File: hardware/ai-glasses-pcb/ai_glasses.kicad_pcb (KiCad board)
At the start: 4 copper layers, 116 x 22 mm, 55 parts, among them J1 USB-C, J2 CAMERA DVP, J3 LiPo 1S, Q1 DMG3415U, SW1 BOOT, SW2 RESET, U1 ESP32-S3-WROOM-1-N16R8, U2 MCP73831-2-OT, U3 AP2112K-3.3, U4 TLV70028DDCR, U5 TLV70012DDCR, U6 ICS-43434, U7 MAX98357A, U8 USBLC6-2SC6

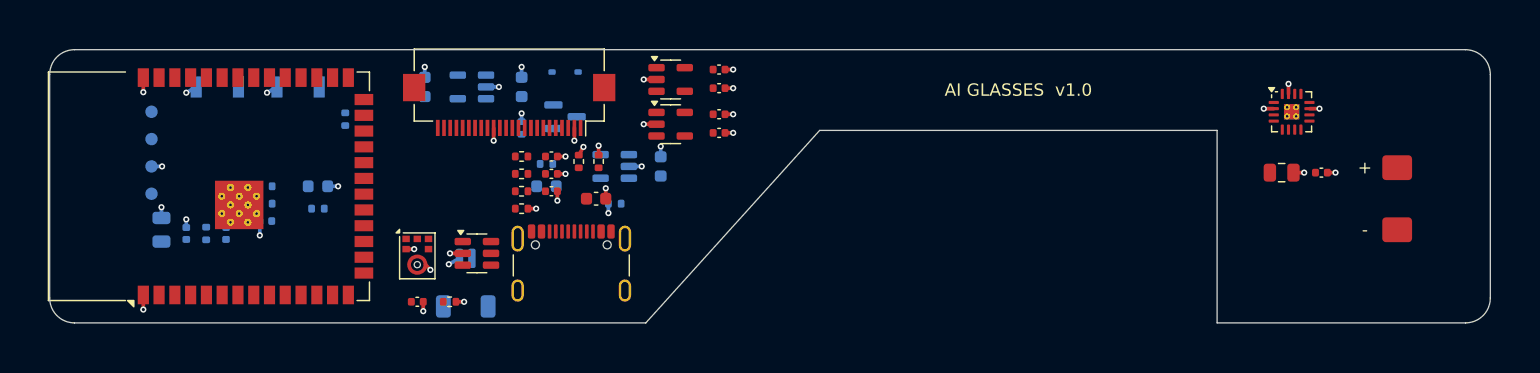
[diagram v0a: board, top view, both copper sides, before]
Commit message: AI glasses PCB: fully routed board, fab outputs, verification
- 116 x 22 mm 4-layer temple board shaped from adult head/ear
  anthropometry (front, taper, 6.5 mm strip over the ear, rear pad
  behind the ear on the mastoid)
- Fully routed: KiCad DRC 0 errors / 0 warnings / 0 unconnected
- check_design.py: 612 checks pass (design = schematic = PCB netlist,
  ERC-style checks, circuit rules, placement/antenna/mic-port checks)
- Gerbers, drill, pick-and-place, BOM, schematic/assembly PDFs in fab/
- Fallback A* router for connections Freerouting leaves open

Co-Authored-By: Claude Opus 5.5 <noreply@anthropic.com>
Claude-Session: https://claude.ai/code/session_018PJ1sVCZoxAbR5ac4Gx3WA
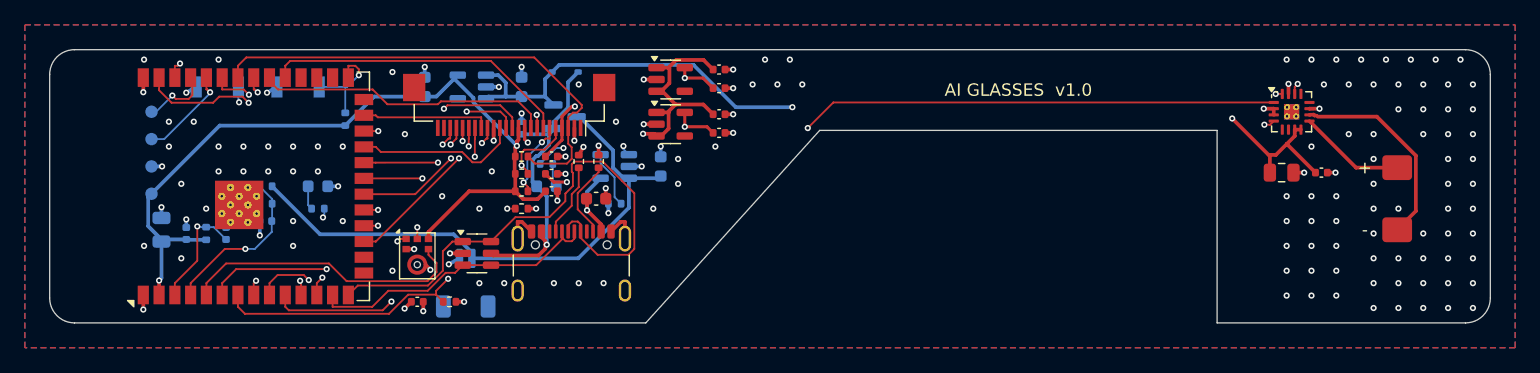
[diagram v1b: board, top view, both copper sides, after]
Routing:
- net +3V3: track 0.00 -> 116.0 mm, vias 0 -> 4
- net AMP_LRCLK: track 0.00 -> 92.2 mm, vias 0 -> 2
- net AMP_BCLK: track 0.00 -> 90.8 mm, vias 0 -> 2
- net AMP_DIN: track 0.00 -> 88.0 mm, vias 0 -> 2
- net AMP_SD: track 0.00 -> 85.8 mm, vias 0 -> 2
- net VSYS: track 0.00 -> 80.3 mm, vias 0 -> 2
- net VBAT: track 0.00 -> 45.2 mm
- net USB_DP: track 0.00 -> 43.3 mm
- net CAM_PWDN: track 0.00 -> 42.4 mm, vias 0 -> 3
- net CAM_RESET: track 0.00 -> 40.4 mm, vias 0 -> 3
- net CAM_SIOD: track 0.00 -> 39.5 mm
- net VBUS: track 0.00 -> 35.0 mm, vias 0 -> 2
- net CAM_SIOC: track 0.00 -> 34.6 mm, vias 0 -> 2
- net MIC_SD: track 0.00 -> 26.4 mm, vias 0 -> 2
- net CAM_VSYNC: track 0.00 -> 24.8 mm
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- added copper zone on B.Cu, net GND
- added copper zone on F.Cu, net GND
- added copper zone on In2.Cu, net GND

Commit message: AI glasses PCB: layout review fixes
- USB D+/D- re-routed as a coupled pair through the ESD part
  (0.03 mm mismatch, was 19 mm); other nets' vias kept out from under it
- Amp supply (VSYS) 0.6 mm min, 2 mm trunk + B.Cu pour in the strip;
  C18/C17 moved to U7's VDD pins
- GND stitching on the front half raised to match the rear
- Filleted outline corners; custom DRC rule: tracks/vias >= 0.5 mm from edge
- Mic port 0.6 mm with inner/bottom copper keep-out; battery polarity silk
- Baseline/final DRC + ERC-equivalent reports in reports/

Co-Authored-By: Claude Opus 5.5 <noreply@anthropic.com>
Claude-Session: https://claude.ai/code/session_018PJ1sVCZoxAbR5ac4Gx3WA
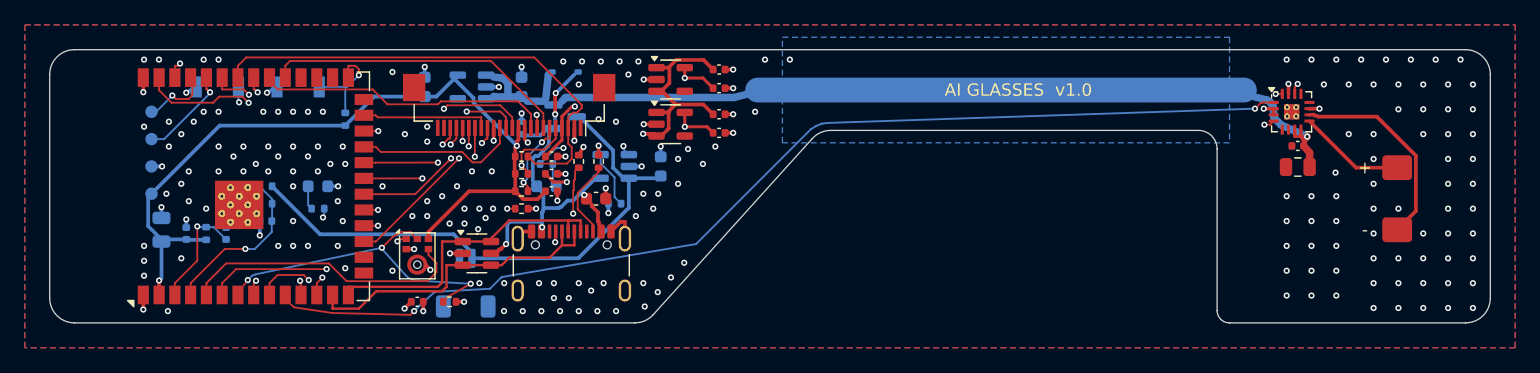
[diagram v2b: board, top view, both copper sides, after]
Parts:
- moved C18 2.87 mm to (150.5, 57.8), turned to 180 degrees
- moved C17 1.38 mm to (150.5, 59.5), turned to 180 degrees
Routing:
- net USB_DP: track 43.3 -> 25.0 mm
- net VBUS: track 35.0 -> 26.0 mm, vias 2 -> 5
- net VSYS: track 80.3 -> 71.9 mm, vias 2 -> 1
- net GND: track 44.0 -> 39.9 mm, vias 156 -> 222
- net AMP_DIN: track 88.0 -> 84.4 mm
- net USB_DM: track 24.0 -> 25.5 mm
- net MIC_SD: track 26.4 -> 25.3 mm, vias 2 -> 3
- net CC1: track 5.90 -> 6.71 mm, vias 0 -> 2
- added copper zone on B.Cu, net VSYS
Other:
- outline, holes or cut-outs redrawn
- board text added: "+"
- board text added: "-"
